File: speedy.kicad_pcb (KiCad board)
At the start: 2 copper layers, 159.2 x 100 mm, 249 parts, among them IC1 TC4424EPA, IC3 VR, IC4 SP721, IC5 LTV827, IC7 TC4424EPA, IC8 TC4424EPA, J1 Conn_02x21_Counter_Clockwise, J2 CONN_01X26, J4 CONN_01X05, Q1 STP62NS04Z, Q10 BC547(b), Q2 STP62NS04Z, Q3 STP62NS04Z, Q4 STP62NS04Z, Q5 STP62NS04Z, Q6 STP62NS04Z, Q7 STP62NS04Z, Q8 STP62NS04Z, Q9 VP3203N3-G, U1 L4940-5V

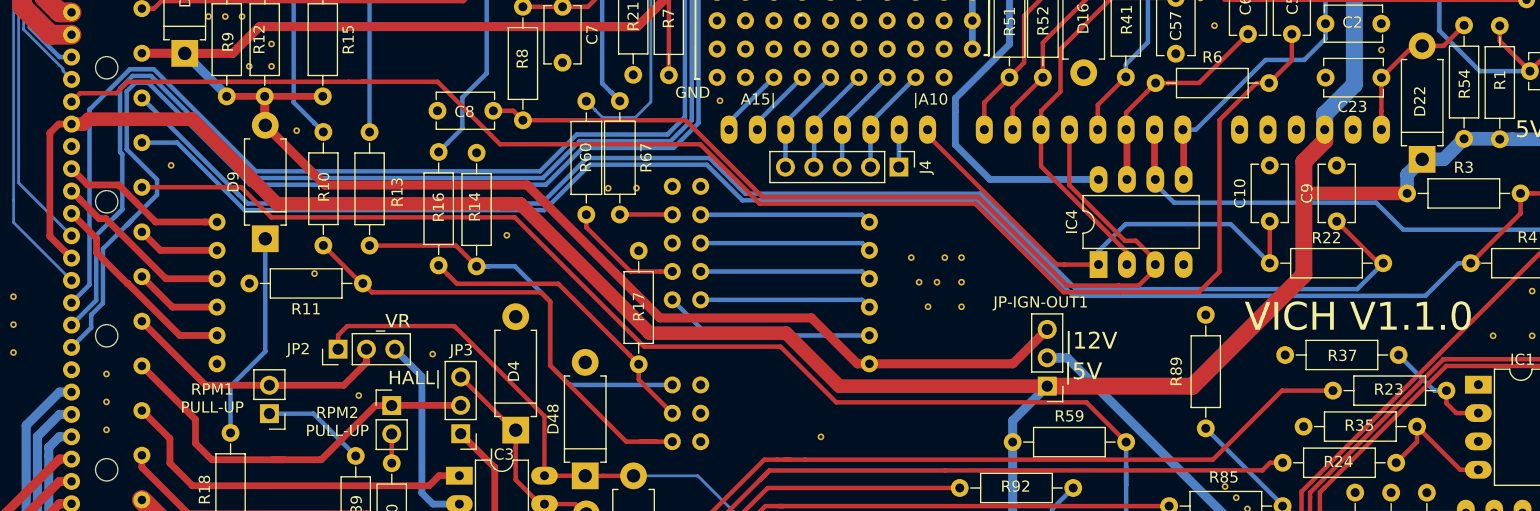
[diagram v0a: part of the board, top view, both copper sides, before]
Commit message: Add mosfet on ULN board
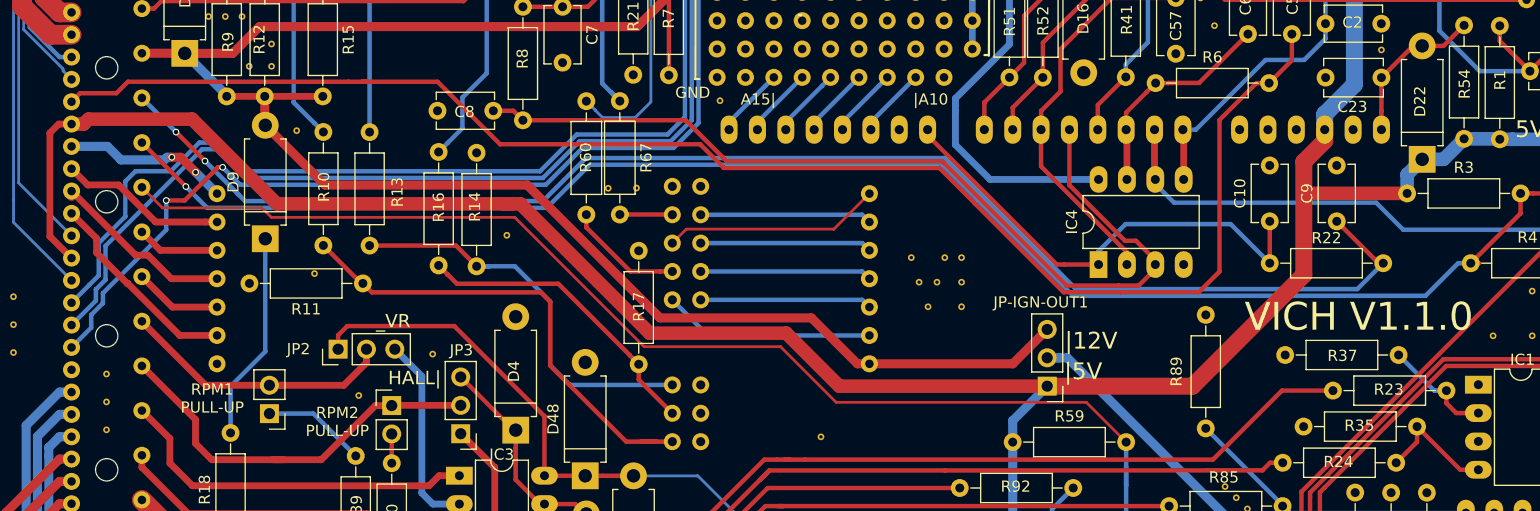
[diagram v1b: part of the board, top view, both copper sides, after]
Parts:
- removed J4: CONN_01X05, Pin_Headers:Pin_Header_Straight_1x05_Pitch2.54mm
- removed the REF** at (82.6, 100.4)
- removed SHIELD2: ULN_SHIELD, conTE42:ULN_SHIELD
- added ULN-SHIELD1: SHIELD2, conTE42:ULN_SHIELD, F.Cu at (86.7, 118.5)
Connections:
- J1 pad 32: ULN-BOOST-OUT -> ULN-FAN2-OUT
- J1 pad 34: GND -> ULN-BOOST-OUT
- SHIELD1 pad 46: ULN-AUX4 -> ULN-FP
- SHIELD1 pad 47: ULN-AUX3 -> ULN-FAN2
- SHIELD1 pad 50: ULN-AUX2 -> ULN-FAN
- SHIELD1 pad 51: Net-(SHIELD1-Pad51) -> ULN-BOOST
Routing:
- net ULN-BOOST: track 0.00 -> 19.5 mm
- net ULN-FAN2: track 0.00 -> 19.4 mm
- net ULN-AUX3: track 19.4 -> 0.00 mm
- net AUX1: track 113.4 -> 96.4 mm, vias 0 -> 2
- net ULN-FAN2-OUT: track 0.00 -> 16.8 mm
- net ULN-FP: track 0.00 -> 15.4 mm
- net ULN-AUX4: track 15.4 -> 0.00 mm
- net ULN-FAN: track 0.00 -> 15.4 mm
- net ULN-AUX2: track 15.4 -> 0.00 mm
- net AUX2: track 113.9 -> 99.7 mm
- net AUX3: track 114.7 -> 103.1 mm
- net AD12: track 10.3 -> 6.91 mm
- net AD13: track 10.8 -> 7.42 mm
- net AD11: track 10.8 -> 7.42 mm
- net AD9: track 3.39 -> 0.04 mm
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
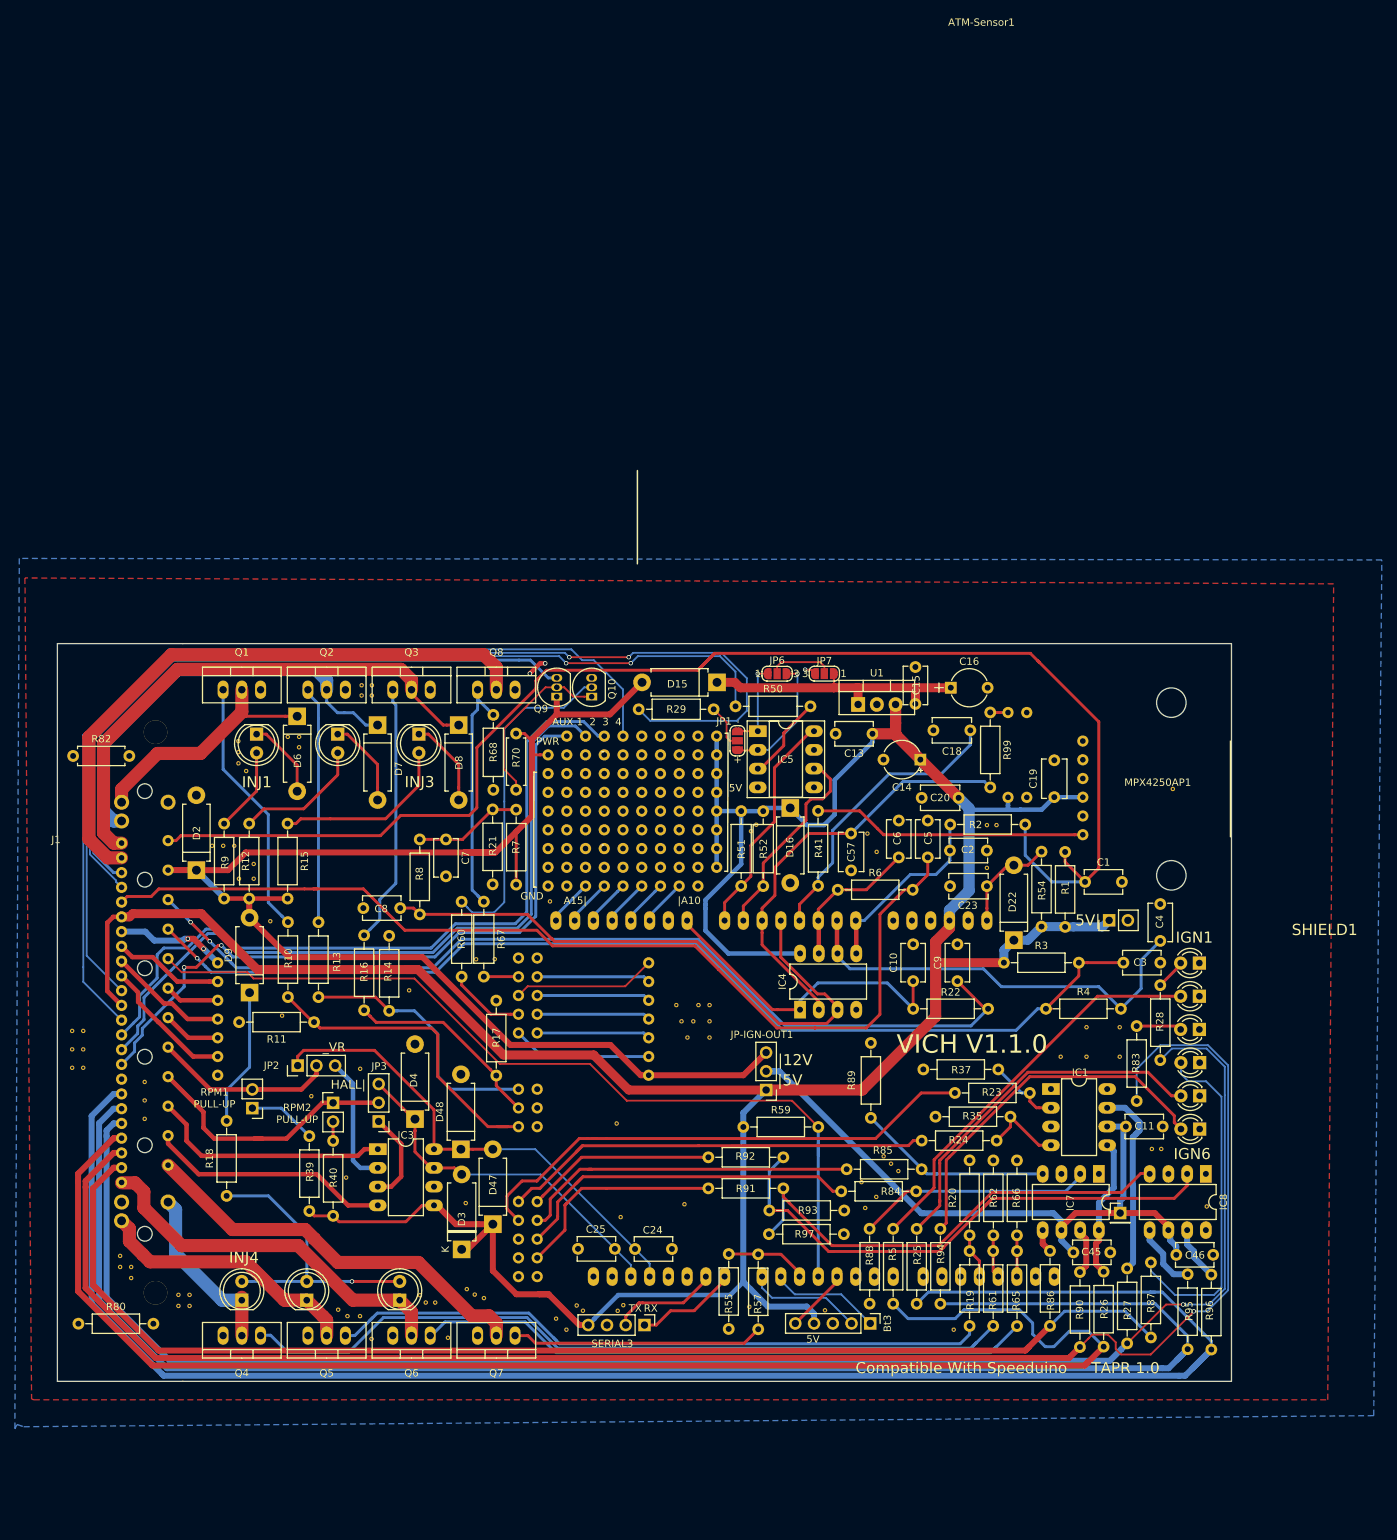
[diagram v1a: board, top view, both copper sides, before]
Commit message: Updated bom and footprint in ULN
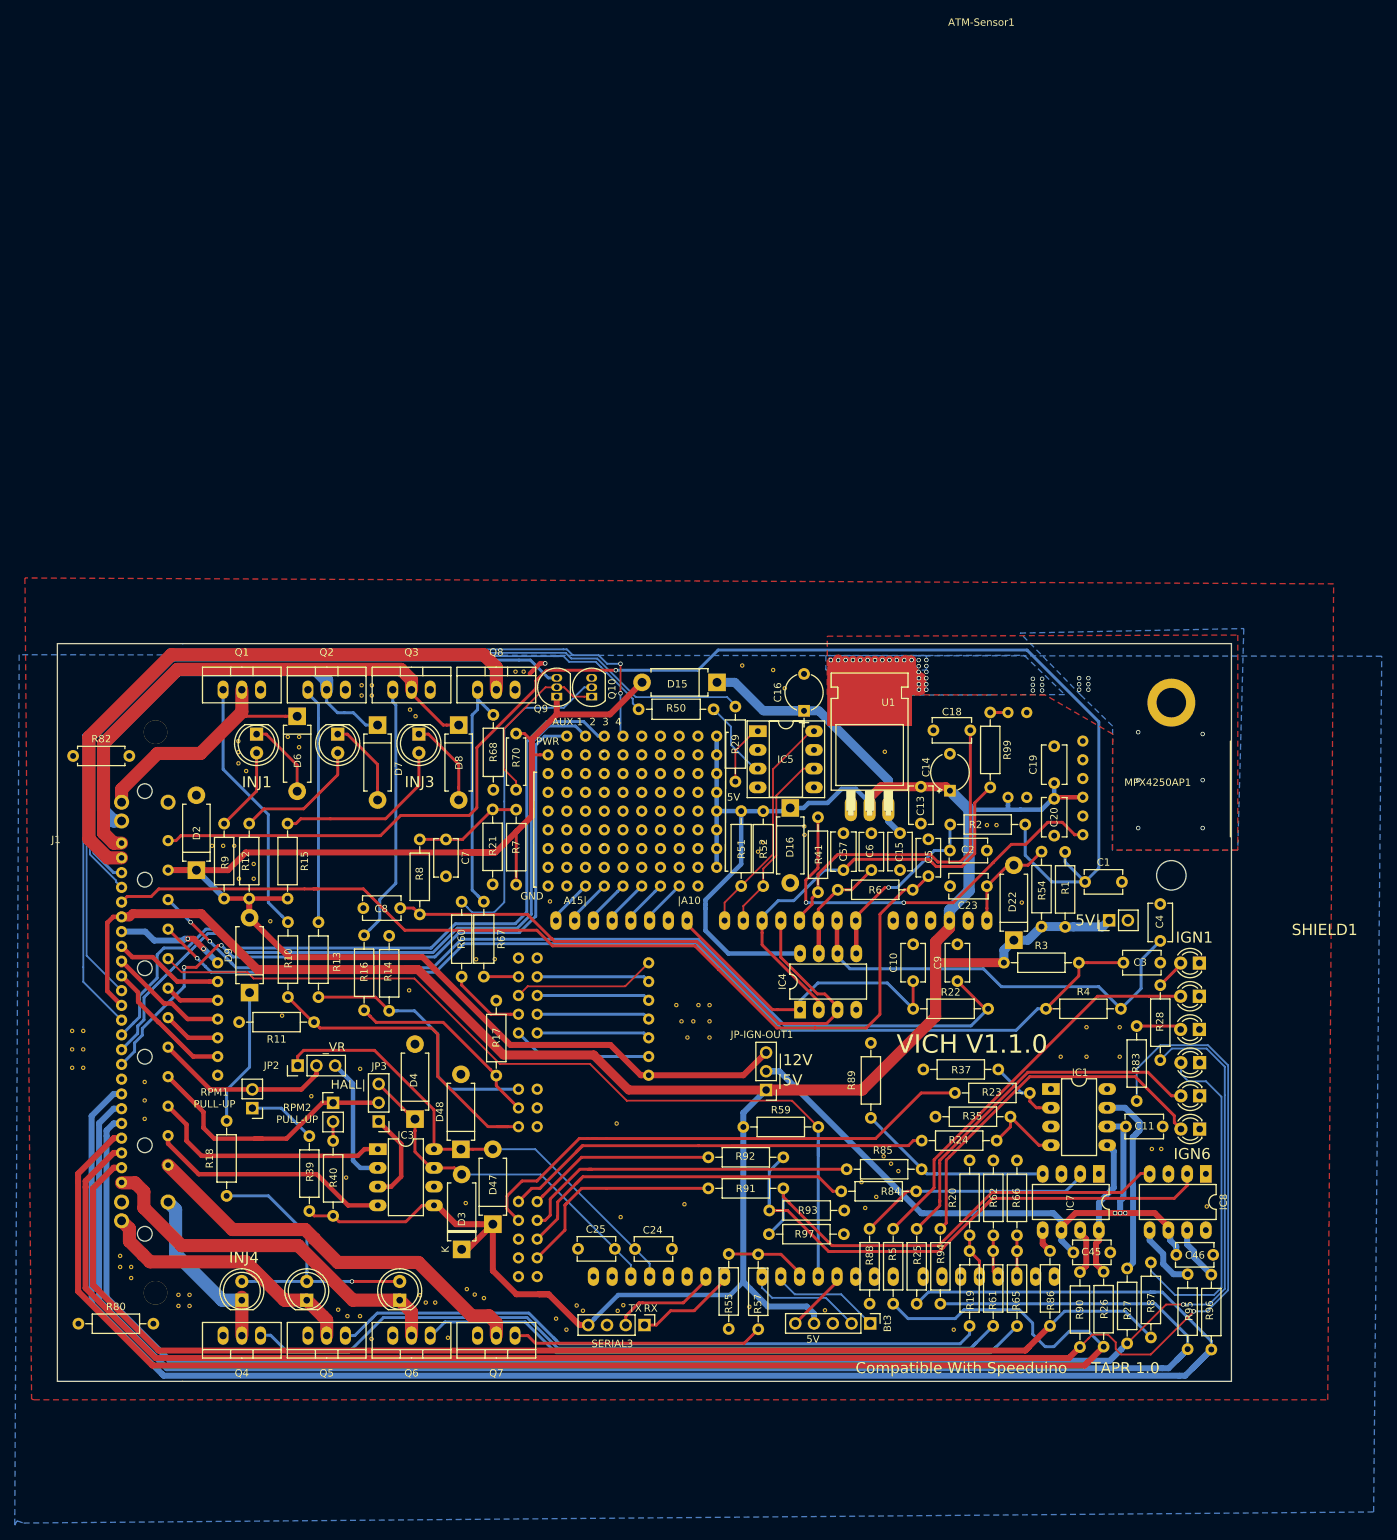
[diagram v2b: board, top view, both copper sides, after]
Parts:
- removed JP1, JP6, JP7: SolderJumper_3_Bridged123, Jumper:SolderJumper-3_P1.3mm_Open_RoundedPad1.0x1.5mm_NumberLabels
- removed the REF** at (176.1, 88.2)
- removed the REF** at (174.8, 85.8)
- removed the REF** at (191.0, 90.4)
- removed the REF** at (216.2, 79.7)
- removed dummyPad1: Conn_01x01, Pin_Headers:Pin_Header_Straight_1x01_Pitch2.54mm
- added REF**: VIA-0.6mm, conTE42:VIA-0.6mm, F.Cu at (177.2, 74.7)
- added REF**: VIA-0.6mm, conTE42:VIA-0.6mm, F.Cu at (166.3, 85.9)
- added REF**: VIA-0.6mm, conTE42:VIA-0.6mm, F.Cu at (166.2, 84.8)
- added REF**: VIA-0.6mm, conTE42:VIA-0.6mm, F.Cu at (195.7, 95.1)
- added REF**: VIA-0.6mm, conTE42:VIA-0.6mm, F.Cu at (157.8, 63.0)
- added REF**: VIA-0.6mm, conTE42:VIA-0.6mm, F.Cu at (162.0, 63.6)
- added REF**: VIA-0.6mm, conTE42:VIA-0.6mm, F.Cu at (163.6, 66.1)
- added REF**: VIA-0.6mm, conTE42:VIA-0.6mm, F.Cu at (128.2, 63.8)
- added REF**: VIA-0.6mm, conTE42:VIA-0.6mm, F.Cu at (127.1, 63.8)
- added REF**: VIA-0.6mm, conTE42:VIA-0.6mm, F.Cu at (113.5, 69.8)
- added REF**: VIA-0.6mm, conTE42:VIA-0.6mm, F.Cu at (112.8, 69.0)
- U1: value L4940-5V -> LD1085-5V; footprint Package_TO_SOT_THT:TO-220-3_Vertical -> conTE42:TO220H
- moved C16 20.1 mm to (166.2, 69.1), turned to 90 degrees
- moved C15 17.6 mm to (179.2, 85.7), turned to 270 degrees
- moved R50 13.1 mm to (143.8, 68.9)
- moved C20 13.0 mm to (200.1, 81.0), turned to 270 degrees
- moved R29 10.2 mm to (156.9, 78.7), turned to 90 degrees
- moved C13 9.73 mm to (182.1, 79.4), turned to 270 degrees
- moved C14 5.82 mm to (186.0, 79.9), turned to 90 degrees
- moved C57 5.07 mm to (171.6, 90.7), turned to 90 degrees
- moved U1 4.29 mm to (175.1, 72.2)
- moved C6 4.09 mm to (175.3, 90.7)
- moved REF** 2.93 mm to (160.0, 88.2)
- moved REF** 2.57 mm to (160.7, 87.0)
- moved C5 2.54 mm to (183.1, 91.5)
- moved C19 1.90 mm to (200.1, 78.9)
- moved R41 0.87 mm to (168.1, 83.5)
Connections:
- IC5 pad 2: Net-(IC5-Pad2) -> GND
- R29 pad 1: Net-(JP1-Pad2) -> Net-(IC5-Pad1)
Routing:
- net 5V: track 448.1 -> 535.9 mm, vias 0 -> 42
- net AUX1-IN: track 152.8 -> 132.0 mm, vias 2 -> 0
- net Net-(MPX4250AP1-Pad1): track 37.2 -> 55.0 mm, vias 0 -> 2
- net Net-(IC5-Pad2): track 17.7 -> 0.00 mm, vias 1 -> 0
- net DINx: track 120.5 -> 105.3 mm, vias 2 -> 0
- net Net-(JP6-Pad2): track 8.87 -> 0.00 mm
- net MAP-CPU-A3: track 39.8 -> 47.6 mm
- net Net-(JP1-Pad2): track 6.19 -> 0.00 mm
- net ADC-Clamp3: track 19.8 -> 15.4 mm
- net Net-(IC5-Pad1): track 11.9 -> 8.32 mm, vias 1 -> 0
- net ADC-Clamp5: track 57.5 -> 60.9 mm
- net 12V: track 38.7 -> 42.0 mm
- net IAT-Sensor: track 190.8 -> 187.7 mm, vias 0 -> 1
- net TPS-Sensor: track 137.3 -> 134.9 mm
- net AUX4: track 127.3 -> 129.2 mm, vias 0 -> 2
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- added copper zone on B.Cu, net 5V
- added copper zone on F.Cu, net 5V
